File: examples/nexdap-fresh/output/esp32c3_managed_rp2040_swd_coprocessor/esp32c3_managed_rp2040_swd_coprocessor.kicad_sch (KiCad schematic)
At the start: 0 parts

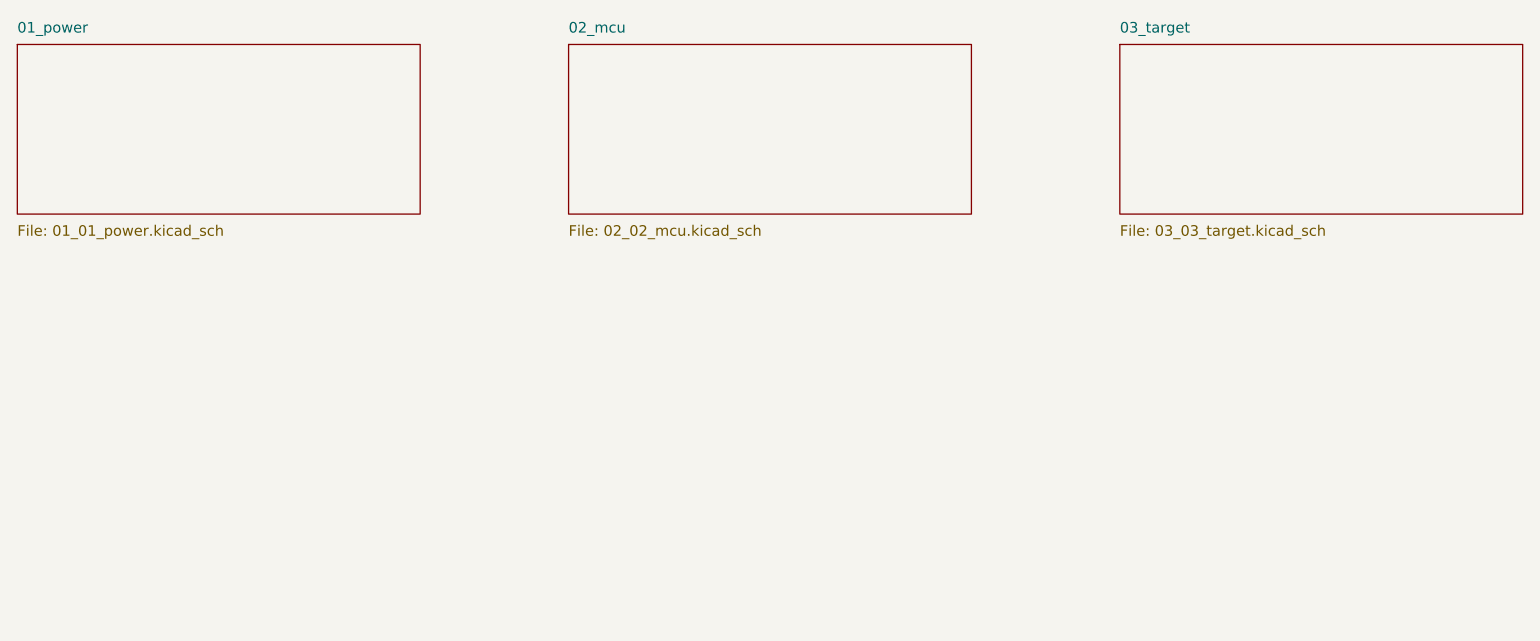
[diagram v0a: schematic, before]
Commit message: Update NexDAP example outputs and fix KiCad mapping logic / 更新 NexDAP 示例输出并修正 KiCad 映射逻辑
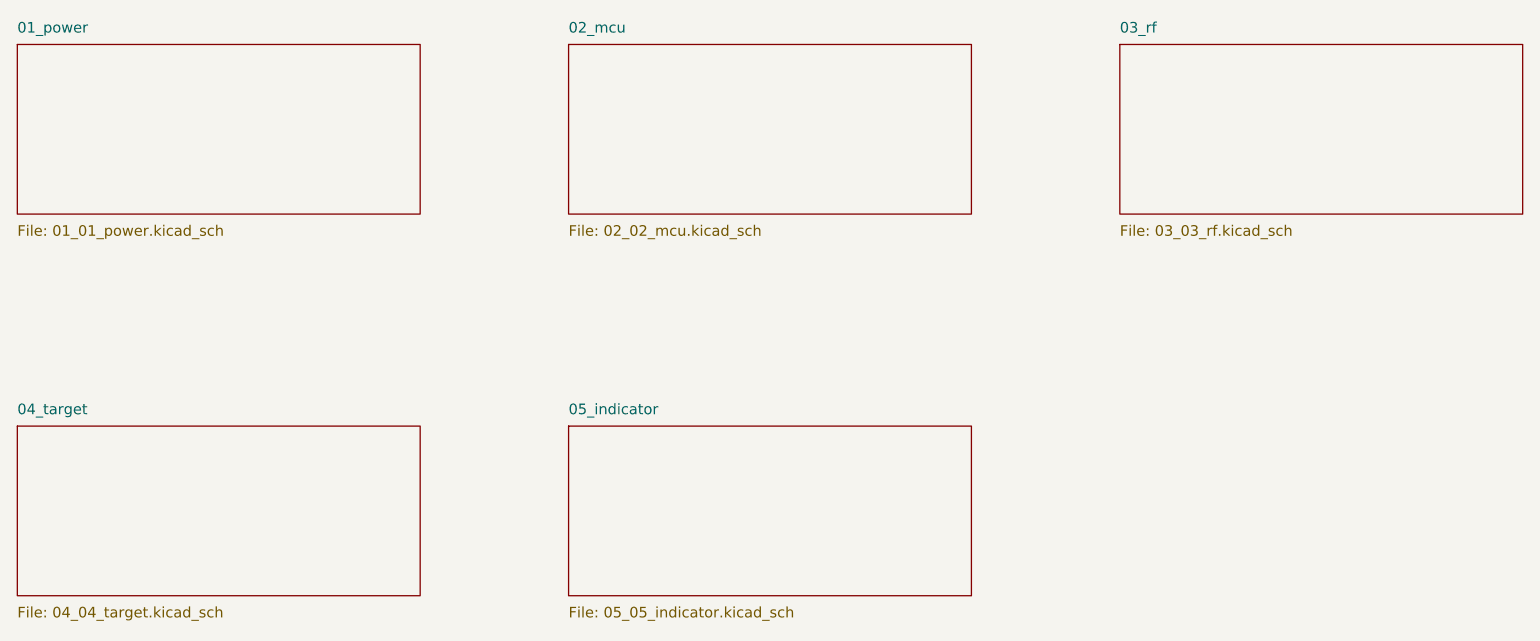
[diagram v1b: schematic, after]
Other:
- removed sheet 03_target
- added sheet 03_rf (03_03_rf.kicad_sch)
- added sheet 04_target (04_04_target.kicad_sch)
- added sheet 05_indicator (05_05_indicator.kicad_sch)
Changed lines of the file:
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@@
 	(paper "A4")
+	(sheet
+		(at 157.48 25.4)
+		(size 48.26 20.32)
+		(exclude_from_sim no)
+		(in_bom yes)
+		(on_board yes)
+		(dnp no)
+		(stroke
+			(width 0.1524)
+			(type solid)
+		)
+		(fill
+			(color 0 0 0 0)
+		)
+		(property "Sheetname" "03_rf"
+			(at 157.48 24.13 0)
+			(show_name no)
+			(do_not_autoplace no)
+			(effects
+				(font
+					(size 1.27 1.27)
+				)
+				(justify left bottom)
+			)
+		)
+		(property "Sheetfile" "03_03_rf.kicad_sch"
+			(at 157.48 46.99 0)
+			(show_name no)
+			(do_not_autoplace no)
+			(effects
+				(font
+					(size 1.27 1.27)
+				)
+				(justify left top)
+			)
+		)
+	)
+	(sheet
+		(at 25.4 71.12)
+		(size 48.26 20.32)
+		(exclude_from_sim no)
+		(in_bom yes)
+		(on_board yes)
+		(dnp no)
+		(stroke
+			(width 0.1524)
+			(type solid)
+		)
+		(fill
+			(color 0 0 0 0)
+		)
+		(property "Sheetname" "04_target"
+			(at 25.4 69.85 0)
+			(show_name no)
+			(do_not_autoplace no)
+			(effects
+				(font
+					(size 1.27 1.27)
+				)
+				(justify left bottom)
+			)
+		)
+		(property "Sheetfile" "04_04_target.kicad_sch"
+			(at 25.4 92.71 0)
+			(show_name no)
+			(do_not_autoplace no)
+			(effects
+				(font
+					(size 1.27 1.27)
+				)
+				(justify left top)
+			)
+		)
+	)
+	(sheet
+		(at 91.44 71.12)
+		(size 48.26 20.32)
+		(exclude_from_sim no)
+		(in_bom yes)
+		(on_board yes)
+		(dnp no)
+		(stroke
+			(width 0.1524)
+			(type solid)
+		)
+		(fill
+			(color 0 0 0 0)
+		)
+		(property "Sheetname" "05_indicator"
+			(at 91.44 69.85 0)
+			(show_name no)
+			(do_not_autoplace no)
+			(effects
+				(font
+					(size 1.27 1.27)
+				)
+				(justify left bottom)
+			)
+		)
+		(property "Sheetfile" "05_05_indicator.kicad_sch"
+			(at 91.44 92.71 0)
+			(show_name no)
+			(do_not_autoplace no)
+			(effects
+				(font
+					(size 1.27 1.27)
+				)
+				(justify left top)
+			)
+		)
+	)
 	(sheet
 		(at 25.4 25.4)
@@
 			(show_name no)
 			(do_not_autoplace no)
-			(effects
-				(font
-					(size 1.27 1.27)
-				)
-				(justify left top)
-			)
-		)
-	)
-	(sheet
-		(at 157.48 25.4)
-		(size 48.26 20.32)
-		(exclude_from_sim no)
-		(in_bom yes)
-		(on_board yes)
-		(dnp no)
-		(stroke
-			(width 0.1524)
-			(type solid)
-		)
-		(fill
-			(color 0 0 0 0)
-		)
-		(property "Sheetname" "03_target"
-			(at 157.48 24.13 0)
-			(show_name no)
-			(do_not_autoplace no)
-			(effects
-				(font
-					(size 1.27 1.27)
-				)
-				(justify left bottom)
-			)
-		)
-		(property "Sheetfile" "03_03_target.kicad_sch"
-			(at 157.48 46.99 0)
-			(show_name no)
-			(do_not_autoplace no)
